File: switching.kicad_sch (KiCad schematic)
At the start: 16 parts, among them K1 SANYOU_SRD_Form_C, K2 SANYOU_SRD_Form_C, Q2 S8050_SMD, Q3 S8050_SMD

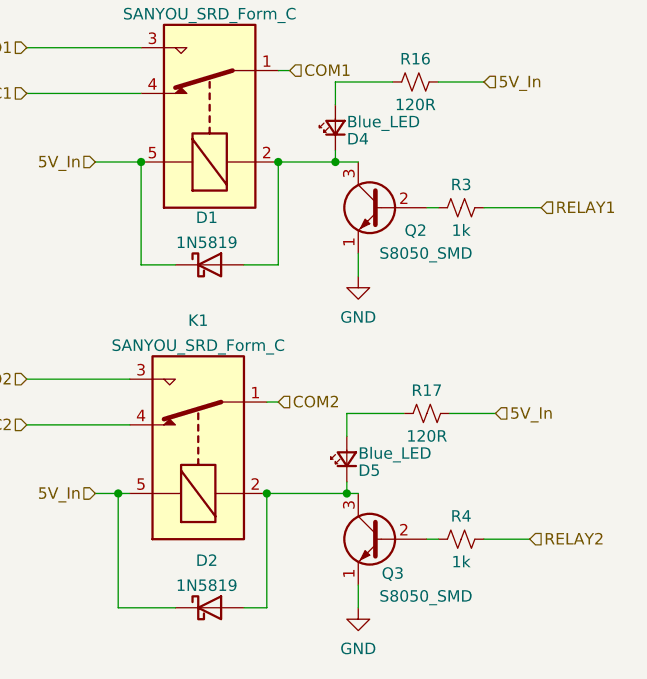
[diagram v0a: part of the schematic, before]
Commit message: Update BJT symbols and ver number
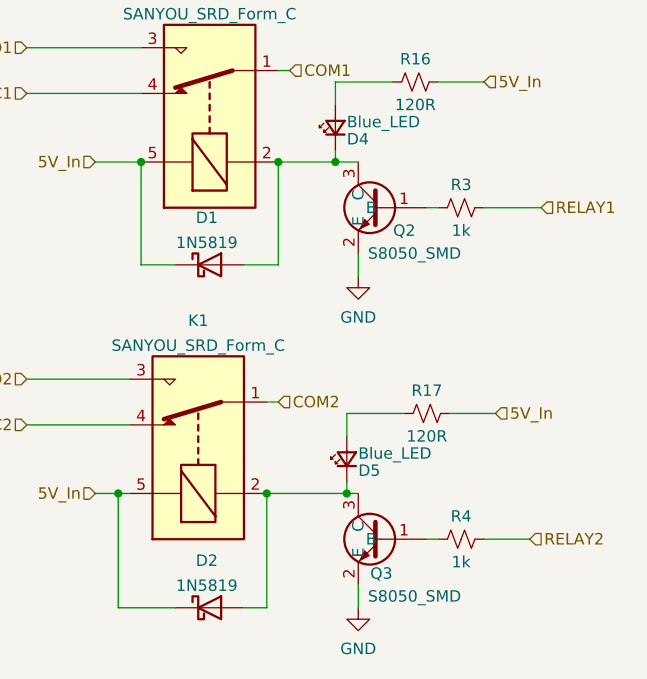
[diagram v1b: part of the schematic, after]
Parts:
- Q2, Q3: symbol Transistor_BJT:S8050 -> UCT:S8050_SMD
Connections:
- net GND: now also Q2.2 (E), Q3.2 (E); no longer Q2.1 (E), Q3.1 (E)
- net at R4.1: now also Q3.1 (B); no longer Q3.2 (B)
- net at R3.1: now also Q2.1 (B); no longer Q2.2 (B)
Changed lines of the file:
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@@
   (paper "A4")
   (title_block
-    (rev "1.1.0")
+    (rev "1.2.0")
   )
   (junction (at 83.82 107.95) (diameter 0) (color 0 0 0 0)
@@
     (stroke (width 0) (type default))
   )
+  (wire (pts (xy 170.18 102.87) (xy 181.61 102.87))
+    (stroke (width 0) (type default))
+  )
+  (wire (pts (xy 87.63 74.93) (xy 110.49 74.93))
+    (stroke (width 0) (type default))
+  )
+  (wire (pts (xy 196.85 115.57) (xy 205.74 115.57))
+    (stroke (width 0) (type default))
+  )
+  (wire (pts (xy 73.66 81.28) (xy 83.82 81.28))
+    (stroke (width 0) (type default))
+  )
+  (wire (pts (xy 204.47 69.85) (xy 210.82 69.85))
+    (stroke (width 0) (type default))
+  )
   (wire (pts (xy 214.63 83.82) (xy 215.9 83.82))
-    (stroke (width 0) (type default))
-  )
-  (wire (pts (xy 170.18 102.87) (xy 181.61 102.87))
-    (stroke (width 0) (type default))
-  )
-  (wire (pts (xy 87.63 74.93) (xy 110.49 74.93))
-    (stroke (width 0) (type default))
-  )
-  (wire (pts (xy 196.85 115.57) (xy 205.74 115.57))
-    (stroke (width 0) (type default))
-  )
-  (wire (pts (xy 73.66 81.28) (xy 83.82 81.28))
-    (stroke (width 0) (type default))
-  )
-  (wire (pts (xy 204.47 69.85) (xy 210.82 69.85))
     (stroke (width 0) (type default))
   )
@@
     )
   )
-  (symbol (lib_id "Transistor_BJT:S8050") (at 209.55 120.65 0) (mirror y) (unit 1)
+  (symbol (lib_id "UCT:S8050_SMD") (at 208.28 120.65 0) (mirror y) (unit 1)
     (in_bom yes) (on_board yes) (dnp no)
-    (property "Reference" "Q3" (at 212.09 124.46 0)
-      (effects (font (size 1.27 1.27)) (justify left))
-    )
-    (property "Value" "S8050_SMD" (at 219.71 127 0)
-      (effects (font (size 1.27 1.27)) (justify left))
-    )
-    (property "Footprint" "Package_TO_SOT_SMD:SOT-23" (at 204.47 122.555 0)
-      (effects (font (size 1.27 1.27) italic) (justify left) hide)
-    )
-    (property "Datasheet" "http://www.unisonic.com.tw/datasheet/S8050.pdf" (at 209.55 120.65 0)
-      (effects (font (size 1.27 1.27)) (justify left) hide)
-    )
-    (property "Populate" "1" (at 209.55 120.65 0)
-      (effects (font (size 1.27 1.27)) hide)
-    )
-    (property "Extended" "0" (at 209.55 120.65 0)
-      (effects (font (size 1.27 1.27)) hide)
-    )
-    (property "LCSC" "C2150" (at 209.55 120.65 0)
+    (property "Reference" "Q3" (at 210.82 124.46 0)
+      (effects (font (size 1.27 1.27)) (justify left))
+    )
+    (property "Value" "S8050_SMD" (at 218.44 127 0)
+      (effects (font (size 1.27 1.27)) (justify left))
+    )
+    (property "Footprint" "Package_TO_SOT_SMD:SOT-23" (at 217.7796 100.7364 0)
+      (effects (font (size 1.27 1.27)) hide)
+    )
+    (property "Datasheet" "https://datasheet.lcsc.com/lcsc/2303221100_Jiangsu-Changjing-Electronics-Technology-Co---Ltd--SS8050_C2150.pdf" (at 220.2688 102.4636 0)
+      (effects (font (size 1.27 1.27)) hide)
+    )
+    (property "Populate" "1" (at 208.28 120.65 0)
+      (effects (font (size 1.27 1.27)) hide)
+    )
+    (property "Extended" "0" (at 208.28 120.65 0)
+      (effects (font (size 1.27 1.27)) hide)
+    )
+    (property "LCSC" "C2150" (at 208.28 120.65 0)
       (effects (font (size 1.27 1.27)) hide)
     )
@@
     )
   )
-  (symbol (lib_id "Transistor_BJT:S8050") (at 209.55 83.82 0) (mirror y) (unit 1)
+  (symbol (lib_id "UCT:S8050_SMD") (at 208.28 83.82 0) (mirror y) (unit 1)
     (in_bom yes) (on_board yes) (dnp no)
-    (property "Reference" "Q2" (at 214.63 86.36 0)
-      (effects (font (size 1.27 1.27)) (justify left))
-    )
-    (property "Value" "S8050_SMD" (at 219.71 88.9 0)
-      (effects (font (size 1.27 1.27)) (justify left))
-    )
-    (property "Footprint" "Package_TO_SOT_SMD:SOT-23" (at 204.47 85.725 0)
-      (effects (font (size 1.27 1.27) italic) (justify left) hide)
-    )
-    (property "Datasheet" "http://www.unisonic.com.tw/datasheet/S8050.pdf" (at 209.55 83.82 0)
-      (effects (font (size 1.27 1.27)) (justify left) hide)
-    )
-    (property "Populate" "1" (at 209.55 83.82 0)
-      (effects (font (size 1.27 1.27)) hide)
-    )
-    (property "Extended" "0" (at 209.55 83.82 0)
-      (effects (font (size 1.27 1.27)) hide)
-    )
-    (property "LCSC" "C2150" (at 209.55 83.82 0)
-      (effects (font (size 1.27 1.27)) hide)
-    )
+    (property "Reference" "Q2" (at 213.36 86.36 0)
+      (effects (font (size 1.27 1.27)) (justify left))
+    )
+    (property "Value" "S8050_SMD" (at 218.44 88.9 0)
+      (effects (font (size 1.27 1.27)) (justify left))
+    )
+    (property "Footprint" "Package_TO_SOT_SMD:SOT-23" (at 217.7796 63.9064 0)
+      (effects (font (size 1.27 1.27)) hide)
+    )
+    (property "Datasheet" "https://datasheet.lcsc.com/lcsc/2303221100_Jiangsu-Changjing-Electronics-Technology-Co---Ltd--SS8050_C2150.pdf" (at 220.2688 65.6336 0)
+      (effects (font (size 1.27 1.27)) hide)
+    )
+    (property "Populate" "1" (at 208.28 83.82 0)
+      (effects (font (size 1.27 1.27)) hide)
+    )
+    (property "Extended" "0" (at 208.28 83.82 0)
+      (effects (font (size 1.27 1.27)) hide)
+    )
+    (property "LCSC" "C2150" (at 208.28 83.82 0)
+      (effects (font (size 1.27 1.27)) hide)
+    )

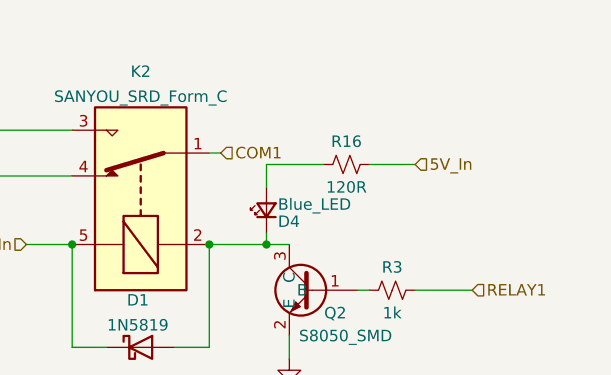
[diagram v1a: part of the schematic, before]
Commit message: Connected NO2 to COM1. Annonated relays.
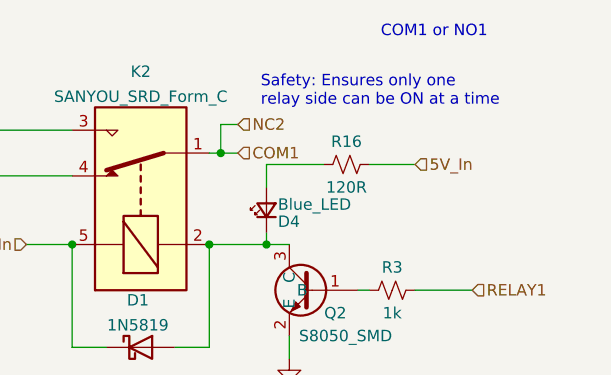
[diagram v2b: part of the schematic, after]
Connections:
- net NC2 is gone; now on net COM1: K1.4
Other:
- note added: "COM1 or NO1"
- note added: "Safety: Ensures only one relay side can be ON at a time"
- title: (none) -> Raspberry Pi Zero Intrumentation HAT
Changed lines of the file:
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@@
   (paper "A4")
   (title_block
-    (rev "1.2.0")
+    (title "Raspberry Pi Zero Intrumentation HAT")
+    (date "2024-06-07")
+    (rev "1.3.0")
+    (comment 1 "@supervisor Justin Pead")
+    (comment 2 "@author Montso Mokake")
   )
   (junction (at 83.82 107.95) (diameter 0) (color 0 0 0 0)
@@
   (junction (at 110.49 101.6) (diameter 0) (color 0 0 0 0)
   )
+  (junction (at 199.39 68.58) (diameter 0) (color 0 0 0 0)
+  )
   (junction (at 204.47 78.74) (diameter 0) (color 0 0 0 0)
   )
@@
     (stroke (width 0) (type default))
   )
+  (wire (pts (xy 199.39 68.58) (xy 201.295 68.58))
+    (stroke (width 0) (type default))
+  )
   (wire (pts (xy 204.47 69.85) (xy 210.82 69.85))
     (stroke (width 0) (type default))
@@
     (stroke (width 0) (type default))
   )
+  (wire (pts (xy 199.39 65.405) (xy 199.39 68.58))
+    (stroke (width 0) (type default))
+  )
   (wire (pts (xy 198.12 78.74) (xy 204.47 78.74))
     (stroke (width 0) (type default))
@@
     (stroke (width 0) (type default))
   )
+  (wire (pts (xy 220.98 83.82) (xy 227.33 83.82))
+    (stroke (width 0) (type default))
+  )
+  (wire (pts (xy 205.74 109.22) (xy 205.74 106.68))
+    (stroke (width 0) (type default))
+  )
+  (wire (pts (xy 73.66 107.95) (xy 83.82 107.95))
+    (stroke (width 0) (type default))
+  )
+  (wire (pts (xy 198.12 90.17) (xy 198.12 78.74))
+    (stroke (width 0) (type default))
+  )
+  (wire (pts (xy 170.18 71.12) (xy 182.88 71.12))
+    (stroke (width 0) (type default))
+  )
+  (wire (pts (xy 194.31 90.17) (xy 198.12 90.17))
+    (stroke (width 0) (type default))
+  )
+  (wire (pts (xy 194.31 128.27) (xy 196.85 128.27))
+    (stroke (width 0) (type default))
+  )
+  (wire (pts (xy 180.34 115.57) (xy 180.34 128.27))
+    (stroke (width 0) (type default))
+  )
+  (wire (pts (xy 205.74 114.3) (xy 205.74 115.57))
+    (stroke (width 0) (type default))
+  )
+  (wire (pts (xy 196.85 128.27) (xy 196.85 115.57))
+    (stroke (width 0) (type default))
+  )
+  (wire (pts (xy 201.295 65.405) (xy 199.39 65.405))
+    (stroke (width 0) (type default))
+  )
+  (wire (pts (xy 182.88 78.74) (xy 182.88 90.17))
+    (stroke (width 0) (type default))
+  )
+  (wire (pts (xy 110.49 69.85) (xy 110.49 74.93))
+    (stroke (width 0) (type default))
+  )
+  (wire (pts (xy 180.34 115.57) (xy 181.61 115.57))
+    (stroke (width 0) (type default))
+  )
+  (wire (pts (xy 220.98 69.85) (xy 215.9 69.85))
+    (stroke (width 0) (type default))
+  )
+  (wire (pts (xy 204.47 77.47) (xy 204.47 78.74))
+    (stroke (width 0) (type default))
+  )
+  (wire (pts (xy 177.8 115.57) (xy 180.34 115.57))
+    (stroke (width 0) (type default))
+  )
+  (wire (pts (xy 207.01 128.27) (xy 207.01 125.73))
+    (stroke (width 0) (type default))
+  )
+  (wire (pts (xy 204.47 78.74) (xy 207.01 78.74))
+    (stroke (width 0) (type default))
+  )
   (wire (pts (xy 170.18 66.04) (xy 182.88 66.04))
     (stroke (width 0) (type default))
   )
-  (wire (pts (xy 220.98 83.82) (xy 227.33 83.82))
-    (stroke (width 0) (type default))
-  )
-  (wire (pts (xy 205.74 109.22) (xy 205.74 106.68))
-    (stroke (width 0) (type default))
-  )
-  (wire (pts (xy 73.66 107.95) (xy 83.82 107.95))
-    (stroke (width 0) (type default))
-  )
-  (wire (pts (xy 198.12 90.17) (xy 198.12 78.74))
-    (stroke (width 0) (type default))
-  )
-  (wire (pts (xy 170.18 71.12) (xy 182.88 71.12))
-    (stroke (width 0) (type default))
-  )
-  (wire (pts (xy 194.31 90.17) (xy 198.12 90.17))
-    (stroke (width 0) (type default))
-  )
-  (wire (pts (xy 194.31 128.27) (xy 196.85 128.27))
-    (stroke (width 0) (type default))
-  )
-  (wire (pts (xy 180.34 115.57) (xy 180.34 128.27))
-    (stroke (width 0) (type default))
-  )
-  (wire (pts (xy 205.74 114.3) (xy 205.74 115.57))
-    (stroke (width 0) (type default))
-  )
-  (wire (pts (xy 196.85 128.27) (xy 196.85 115.57))
-    (stroke (width 0) (type default))
-  )
-  (wire (pts (xy 182.88 78.74) (xy 182.88 90.17))
-    (stroke (width 0) (type default))
-  )
-  (wire (pts (xy 110.49 69.85) (xy 110.49 74.93))
-    (stroke (width 0) (type default))
-  )
-  (wire (pts (xy 180.34 115.57) (xy 181.61 115.57))
-    (stroke (width 0) (type default))
-  )
-  (wire (pts (xy 220.98 69.85) (xy 215.9 69.85))
-    (stroke (width 0) (type default))
-  )
-  (wire (pts (xy 204.47 77.47) (xy 204.47 78.74))
-    (stroke (width 0) (type default))
-  )
-  (wire (pts (xy 177.8 115.57) (xy 180.34 115.57))
-    (stroke (width 0) (type default))
-  )
-  (wire (pts (xy 207.01 128.27) (xy 207.01 125.73))
-    (stroke (width 0) (type default))
-  )
-  (wire (pts (xy 204.47 78.74) (xy 207.01 78.74))
-    (stroke (width 0) (type default))
-  )
   (wire (pts (xy 87.63 101.6) (xy 110.49 101.6))
     (stroke (width 0) (type default))
@@
   (wire (pts (xy 106.68 77.47) (xy 106.68 81.28))
     (stroke (width 0) (type default))
+  )
+  (text "COM1 or NO1" (at 217.17 55.88 0)
+    (effects (font (size 1.27 1.27)) (justify left bottom))
+  )
+  (text "Safety: Ensures only one \nrelay side can be ON at a time"
+    (at 203.835 63.5 0)
+    (effects (font (size 1.27 1.27)) (justify left bottom))
   )
   (hierarchical_label "NO2" (shape input) (at 170.18 102.87 180) (fields_autoplaced)
@@
     (effects (font (size 1.27 1.27)) (justify left))
   )
-  (hierarchical_label "COM1" (shape input) (at 199.39 68.58 0) (fields_autoplaced)
-    (effects (font (size 1.27 1.27)) (justify left))
-  )
+  (hierarchical_label "NC2" (shape input) (at 201.295 65.405 0) (fields_autoplaced)
+    (effects (font (size 1.27 1.27)) (justify left))
+  )
+  (hierarchical_label "COM1" (shape input) (at 201.295 68.58 0) (fields_autoplaced)
+    (effects (font (size 1.27 1.27)) (justify left))
+  )

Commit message: Ammended it to have the jumper connection
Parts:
- added JP13: Jumper_2_Small_Bridged, Jumper:SolderJumper-2_P1.3mm_Bridged_RoundedPad1.0x1.5mm, symbol Jumper:Jumper_2_Small_Bridged
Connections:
- net COM1: no longer K1.4
- net NO1: now also JP13.1 (A)
- new net NC2: JP13.2 (B), K1.4
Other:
- note removed: "COM1 or NO1"

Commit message: Modified the PCB to have a greater spacing on anything Relay 2ndary side related
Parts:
- added JP14, JP15: Jumper_2_Small_Bridged, UCT:Jumper_Open_wide, symbol Jumper:Jumper_2_Small_Bridged
- D4, D5: value Blue_LED -> Red_LED
- R16, R17: value 120R -> 1k; LCSC C25079 -> C11702
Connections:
- net 12V_In: now also JP15.2 (B); no longer JP1.1 (A), JP2.1 (A), JP3.1 (A), JP4.1 (A)
- net 5V_In: now also JP14.2 (B); no longer JP1.3 (B), JP2.3 (B), JP3.3 (B), JP4.3 (B)
- new net: JP1.1 (A), JP15.1 (A), JP2.1 (A), JP3.1 (A), JP4.1 (A)
- new net: JP1.3 (B), JP14.1 (A), JP2.3 (B), JP3.3 (B), JP4.3 (B)
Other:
- moved on the sheet: JP1, JP2, JP3, JP4
